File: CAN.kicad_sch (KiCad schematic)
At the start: 17 parts, among them J8 CAN_IN, J9 CAN_OUT, U6 ADM3055E, U7 CDSOT23-T24CAN

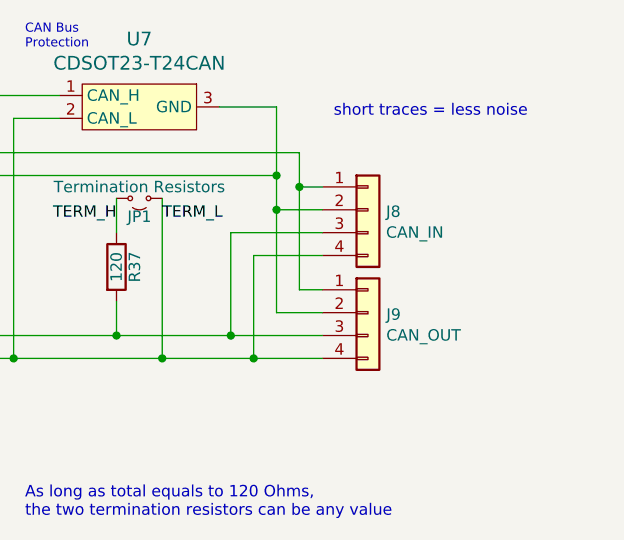
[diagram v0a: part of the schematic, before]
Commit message: parts sheet and cost estimate
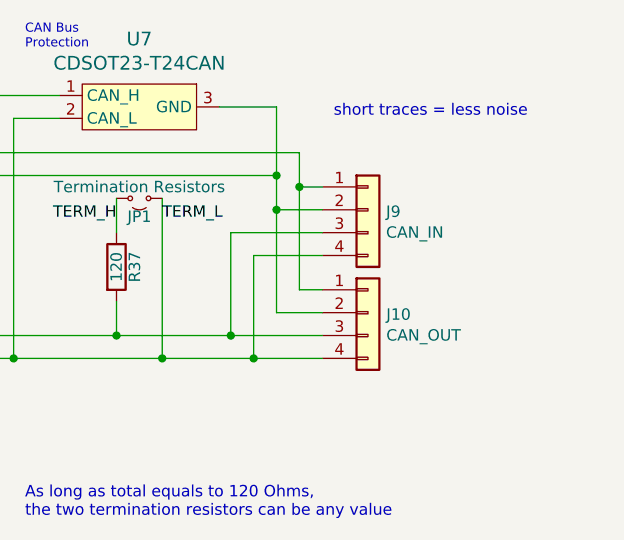
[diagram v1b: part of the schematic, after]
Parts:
- J10: renamed from J9; footprint UTSVT_Connectors:Molex_MicroFit3.0_1x4xP3.00mm_PolarizingPeg_Vertical -> utsvt-conn:Molex_MicroFit3.0_1x4xP3.00mm_PolarizingPeg_Vertical
- J9: renamed from J8; footprint UTSVT_Connectors:Molex_MicroFit3.0_1x4xP3.00mm_PolarizingPeg_Vertical -> utsvt-conn:Molex_MicroFit3.0_1x4xP3.00mm_PolarizingPeg_Vertical
- U6: footprint UTSVT_ICs:SOIC-20W_7.5x15.4mm_Pitch1.27mm -> utsvt-ics:SOIC-20W_7.5x15.4mm_Pitch1.27mm
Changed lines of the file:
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@@
 		(on_board yes)
 		(dnp no)
-		(property "Reference" "J9"
+		(property "Reference" "J10"
 			(at 221.742 92.9132 0)
 			(effects
@@
 			)
 		)
-		(property "Footprint" "UTSVT_Connectors:Molex_MicroFit3.0_1x4xP3.00mm_PolarizingPeg_Vertical"
+		(property "Footprint" "utsvt-conn:Molex_MicroFit3.0_1x4xP3.00mm_PolarizingPeg_Vertical"
 			(at 219.71 92.71 0)
 			(effects
@@
 			(project "ActivePrecharge"
 				(path "/b9847a31-2b3b-47ca-9561-fab506416f6d/a2982df7-4a65-4a2b-8298-6a7a639680dd"
-					(reference "J9")
+					(reference "J10")
 					(unit 1)
 				)
@@
 			)
 		)
-		(property "Footprint" "UTSVT_ICs:SOIC-20W_7.5x15.4mm_Pitch1.27mm"
+		(property "Footprint" "utsvt-ics:SOIC-20W_7.5x15.4mm_Pitch1.27mm"
 			(at 99.06 86.36 0)
 			(effects
@@
 		(on_board yes)
 		(dnp no)
-		(property "Reference" "J8"
+		(property "Reference" "J9"
 			(at 221.7166 81.4832 0)
 			(effects
@@
 			)
 		)
-		(property "Footprint" "UTSVT_Connectors:Molex_MicroFit3.0_1x4xP3.00mm_PolarizingPeg_Vertical"
+		(property "Footprint" "utsvt-conn:Molex_MicroFit3.0_1x4xP3.00mm_PolarizingPeg_Vertical"
 			(at 219.71 81.28 0)
 			(effects
@@
 			(project "ActivePrecharge"
 				(path "/b9847a31-2b3b-47ca-9561-fab506416f6d/a2982df7-4a65-4a2b-8298-6a7a639680dd"
-					(reference "J8")
+					(reference "J9")
 					(unit 1)
 				)

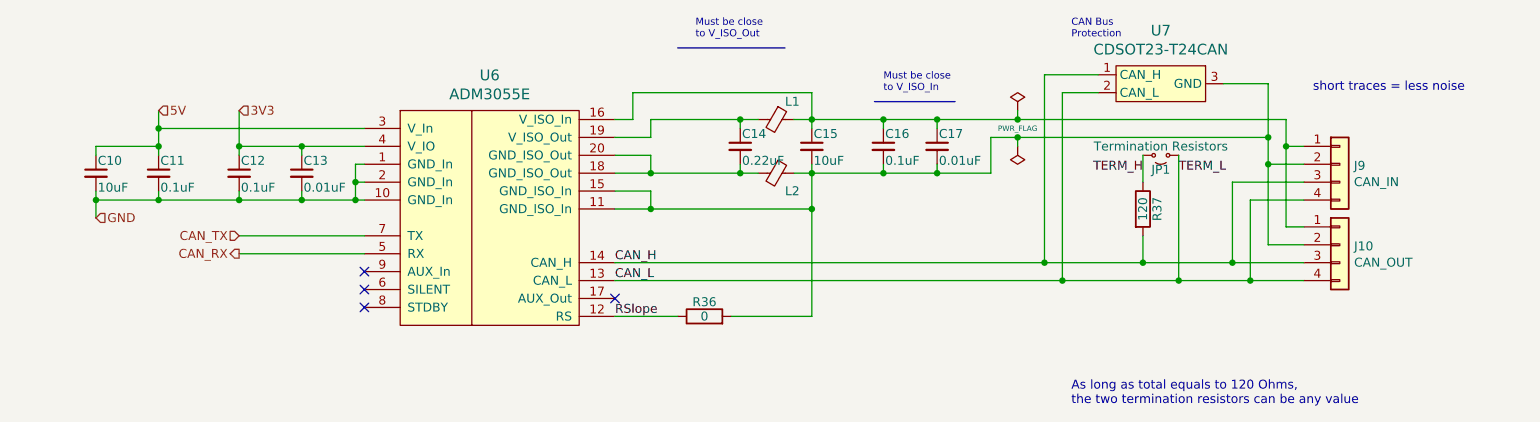
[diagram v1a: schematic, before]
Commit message: started on HV layout
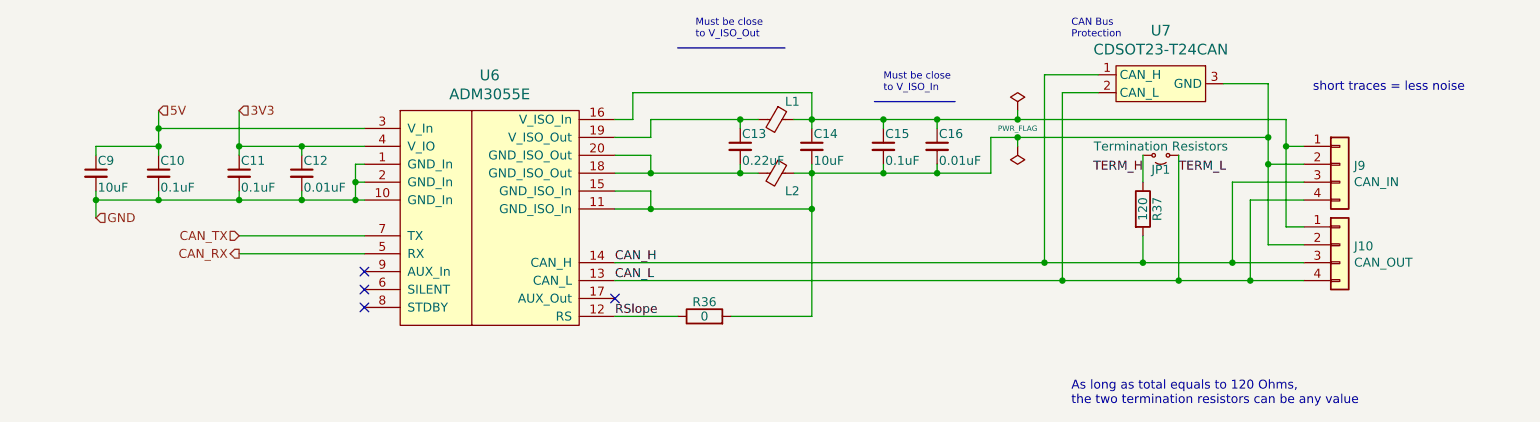
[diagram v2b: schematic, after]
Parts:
- renumbered C11 to C10, C12 to C11, C13 to C12, C14 to C13, C15 to C14, C16 to C15, C17 to C16, C10 to C9
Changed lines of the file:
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@@
 		(on_board yes)
 		(dnp no)
-		(property "Reference" "C13"
+		(property "Reference" "C12"
 			(at 72.644 80.772 0)
 			(effects
@@
 			(project "ActivePrecharge"
 				(path "/b9847a31-2b3b-47ca-9561-fab506416f6d/a2982df7-4a65-4a2b-8298-6a7a639680dd"
-					(reference "C13")
+					(reference "C12")
 					(unit 1)
 				)
@@
 		(on_board yes)
 		(dnp no)
-		(property "Reference" "C17"
+		(property "Reference" "C16"
 			(at 162.814 76.962 0)
 			(effects
@@
 			(project "ActivePrecharge"
 				(path "/b9847a31-2b3b-47ca-9561-fab506416f6d/a2982df7-4a65-4a2b-8298-6a7a639680dd"
-					(reference "C17")
+					(reference "C16")
 					(unit 1)
 				)
@@
 		(on_board yes)
 		(dnp no)
-		(property "Reference" "C10"
+		(property "Reference" "C9"
 			(at 43.434 80.772 0)
 			(effects
@@
 			(project "ActivePrecharge"
 				(path "/b9847a31-2b3b-47ca-9561-fab506416f6d/a2982df7-4a65-4a2b-8298-6a7a639680dd"
-					(reference "C10")
+					(reference "C9")
 					(unit 1)
 				)
@@
 		(on_board yes)
 		(dnp no)
-		(property "Reference" "C12"
+		(property "Reference" "C11"
 			(at 63.754 80.772 0)
 			(effects
@@
 			(project "ActivePrecharge"
 				(path "/b9847a31-2b3b-47ca-9561-fab506416f6d/a2982df7-4a65-4a2b-8298-6a7a639680dd"
-					(reference "C12")
+					(reference "C11")
 					(unit 1)
 				)
@@
 		(on_board yes)
 		(dnp no)
-		(property "Reference" "C11"
+		(property "Reference" "C10"
 			(at 52.324 80.772 0)
 			(effects
@@
 			(project "ActivePrecharge"
 				(path "/b9847a31-2b3b-47ca-9561-fab506416f6d/a2982df7-4a65-4a2b-8298-6a7a639680dd"
-					(reference "C11")
+					(reference "C10")
 					(unit 1)
 				)
@@
 		(on_board yes)
 		(dnp no)
-		(property "Reference" "C14"
+		(property "Reference" "C13"
 			(at 134.874 76.962 0)
 			(effects
@@
 			(project "ActivePrecharge"
 				(path "/b9847a31-2b3b-47ca-9561-fab506416f6d/a2982df7-4a65-4a2b-8298-6a7a639680dd"
-					(reference "C14")
+					(reference "C13")
 					(unit 1)
 				)
@@
 		(on_board yes)
 		(dnp no)
-		(property "Reference" "C16"
+		(property "Reference" "C15"
 			(at 155.194 76.962 0)
 			(effects
@@
 			(project "ActivePrecharge"
 				(path "/b9847a31-2b3b-47ca-9561-fab506416f6d/a2982df7-4a65-4a2b-8298-6a7a639680dd"
-					(reference "C16")
+					(reference "C15")
 					(unit 1)
 				)
@@
 		(on_board yes)
 		(dnp no)
-		(property "Reference" "C15"
+		(property "Reference" "C14"
 			(at 145.034 76.962 0)
 			(effects
@@
 			(project "ActivePrecharge"
 				(path "/b9847a31-2b3b-47ca-9561-fab506416f6d/a2982df7-4a65-4a2b-8298-6a7a639680dd"
-					(reference "C15")
+					(reference "C14")
 					(unit 1)
 				)

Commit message: fixed lakshay and ravi comments, renamed signals to be more readable, further worked on HV side layout
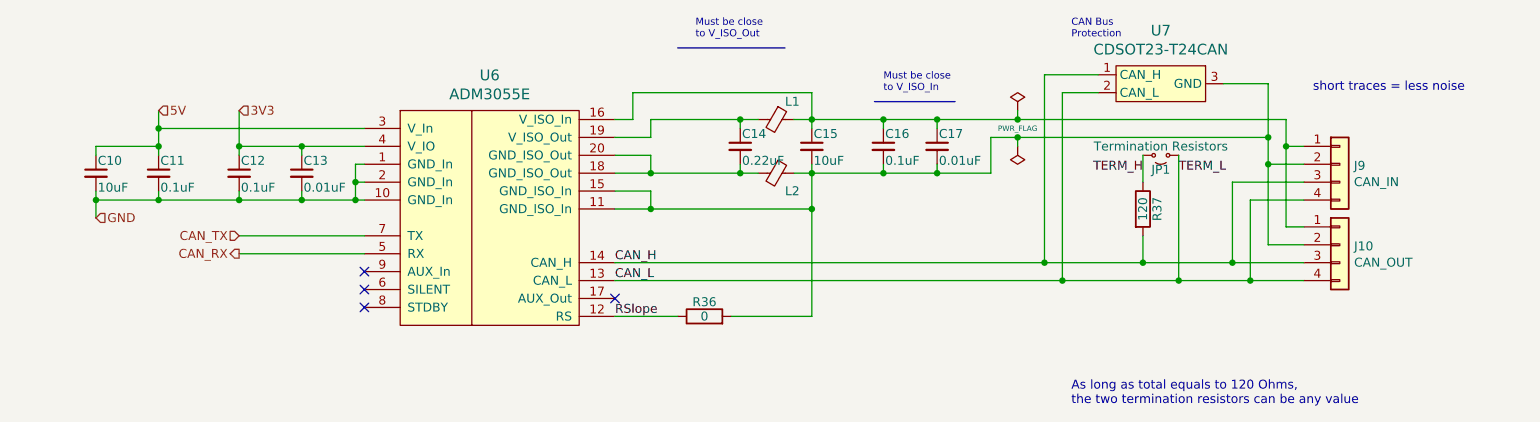
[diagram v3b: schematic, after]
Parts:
- renumbered C9 to C10, C10 to C11, C11 to C12, C12 to C13, C13 to C14, C14 to C15, C15 to C16, C16 to C17
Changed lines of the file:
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@@
 		(on_board yes)
 		(dnp no)
-		(property "Reference" "C12"
+		(property "Reference" "C13"
 			(at 72.644 80.772 0)
 			(effects
@@
 			(project "ActivePrecharge"
 				(path "/b9847a31-2b3b-47ca-9561-fab506416f6d/a2982df7-4a65-4a2b-8298-6a7a639680dd"
-					(reference "C12")
+					(reference "C13")
 					(unit 1)
 				)
@@
 		(on_board yes)
 		(dnp no)
-		(property "Reference" "C16"
+		(property "Reference" "C17"
 			(at 162.814 76.962 0)
 			(effects
@@
 			(project "ActivePrecharge"
 				(path "/b9847a31-2b3b-47ca-9561-fab506416f6d/a2982df7-4a65-4a2b-8298-6a7a639680dd"
-					(reference "C16")
+					(reference "C17")
 					(unit 1)
 				)
@@
 		(on_board yes)
 		(dnp no)
-		(property "Reference" "C9"
+		(property "Reference" "C10"
 			(at 43.434 80.772 0)
 			(effects
@@
 			(project "ActivePrecharge"
 				(path "/b9847a31-2b3b-47ca-9561-fab506416f6d/a2982df7-4a65-4a2b-8298-6a7a639680dd"
-					(reference "C9")
+					(reference "C10")
 					(unit 1)
 				)
@@
 		(on_board yes)
 		(dnp no)
-		(property "Reference" "C11"
+		(property "Reference" "C12"
 			(at 63.754 80.772 0)
 			(effects
@@
 			(project "ActivePrecharge"
 				(path "/b9847a31-2b3b-47ca-9561-fab506416f6d/a2982df7-4a65-4a2b-8298-6a7a639680dd"
-					(reference "C11")
+					(reference "C12")
 					(unit 1)
 				)
@@
 		(on_board yes)
 		(dnp no)
-		(property "Reference" "C10"
+		(property "Reference" "C11"
 			(at 52.324 80.772 0)
 			(effects
@@
 			(project "ActivePrecharge"
 				(path "/b9847a31-2b3b-47ca-9561-fab506416f6d/a2982df7-4a65-4a2b-8298-6a7a639680dd"
-					(reference "C10")
+					(reference "C11")
 					(unit 1)
 				)
@@
 		(on_board yes)
 		(dnp no)
-		(property "Reference" "C13"
+		(property "Reference" "C14"
 			(at 134.874 76.962 0)
 			(effects
@@
 			(project "ActivePrecharge"
 				(path "/b9847a31-2b3b-47ca-9561-fab506416f6d/a2982df7-4a65-4a2b-8298-6a7a639680dd"
-					(reference "C13")
+					(reference "C14")
 					(unit 1)
 				)
@@
 		(on_board yes)
 		(dnp no)
-		(property "Reference" "C15"
+		(property "Reference" "C16"
 			(at 155.194 76.962 0)
 			(effects
@@
 			(project "ActivePrecharge"
 				(path "/b9847a31-2b3b-47ca-9561-fab506416f6d/a2982df7-4a65-4a2b-8298-6a7a639680dd"
-					(reference "C15")
+					(reference "C16")
 					(unit 1)
 				)
@@
 		(on_board yes)
 		(dnp no)
-		(property "Reference" "C14"
+		(property "Reference" "C15"
 			(at 145.034 76.962 0)
 			(effects
@@
 			(project "ActivePrecharge"
 				(path "/b9847a31-2b3b-47ca-9561-fab506416f6d/a2982df7-4a65-4a2b-8298-6a7a639680dd"
-					(reference "C14")
+					(reference "C15")
 					(unit 1)
 				)

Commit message: end of workday, will work on more tonight
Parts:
- renumbered J9 to J8, J10 to J9
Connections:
- net CAN_H: now also J8.2 (Pin_2), J9.2 (Pin_2); no longer J8.3 (Pin_3), J9.3 (Pin_3)
- net CAN_L: now also J8.1 (Pin_1), J9.1 (Pin_1); no longer J8.4 (Pin_4), J9.4 (Pin_4)
- net at C15.1, C16.1, C17.1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: now also J8.4 (Pin_4), J9.4 (Pin_4); no longer J8.1 (Pin_1), J9.1 (Pin_1)
- net at C15.2, C16.2, C17.2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: now also J8.3 (Pin_3), J9.3 (Pin_3); no longer J8.2 (Pin_2), J9.2 (Pin_2)
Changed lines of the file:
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@@
 	(symbol
 		(lib_id "Connector_Generic:Conn_01x04")
-		(at 219.71 92.71 0)
+		(at 219.71 95.25 0)
+		(mirror x)
 		(unit 1)
 		(exclude_from_sim no)
@@
 		(on_board yes)
 		(dnp no)
-		(property "Reference" "J10"
-			(at 221.742 92.9132 0)
+		(property "Reference" "J9"
+			(at 221.742 95.0468 0)
 			(effects
 				(font
@@
 		)
 		(property "Value" "CAN_OUT"
-			(at 221.742 95.2246 0)
+			(at 221.742 92.7354 0)
 			(effects
 				(font
@@
 		)
 		(property "Footprint" "utsvt-conn:Molex_MicroFit3.0_1x4xP3.00mm_PolarizingPeg_Vertical"
-			(at 219.71 92.71 0)
+			(at 219.71 95.25 0)
 			(effects
 				(font
@@
 		)
 		(property "Datasheet" "~"
-			(at 219.71 92.71 0)
+			(at 219.71 95.25 0)
 			(effects
 				(font
@@
 		)
 		(property "Description" "Generic connector, single row, 01x04, script generated (kicad-library-utils/schlib/autogen/connector/)"
-			(at 219.71 92.71 0)
+			(at 219.71 95.25 0)
 			(effects
 				(font
@@
 		)
 		(property "Id" ""
-			(at 219.71 92.71 0)
+			(at 219.71 95.25 0)
 			(effects
 				(font
@@
 		)
 		(property "Vds" ""
-			(at 219.71 92.71 0)
+			(at 219.71 95.25 0)
 			(effects
 				(font
@@
 		)
 		(property "Digikey" ""
-			(at 219.71 92.71 0)
+			(at 219.71 95.25 0)
 			(effects
 				(font
@@
 		)
 		(property "P/N" "436500244"
-			(at 219.71 92.71 0)
+			(at 219.71 95.25 0)
 			(effects
 				(font
@@
 			(project "ActivePrecharge"
 				(path "/b9847a31-2b3b-47ca-9561-fab506416f6d/a2982df7-4a65-4a2b-8298-6a7a639680dd"
-					(reference "J10")
+					(reference "J9")
 					(unit 1)
 				)
@@
 	(symbol
 		(lib_id "Connector_Generic:Conn_01x04")
-		(at 219.71 81.28 0)
+		(at 219.71 83.82 0)
+		(mirror x)
 		(unit 1)
 		(exclude_from_sim no)
@@
 		(on_board yes)
 		(dnp no)
-		(property "Reference" "J9"
-			(at 221.7166 81.4832 0)
+		(property "Reference" "J8"
+			(at 221.7166 83.6168 0)
 			(effects
 				(font
@@
 		)
 		(property "Value" "CAN_IN"
-			(at 221.7166 83.7946 0)
+			(at 221.7166 81.3054 0)
 			(effects
 				(font
@@
 		)
 		(property "Footprint" "utsvt-conn:Molex_MicroFit3.0_1x4xP3.00mm_PolarizingPeg_Vertical"
-			(at 219.71 81.28 0)
+			(at 219.71 83.82 0)
 			(effects
 				(font
@@
 		)
 		(property "Datasheet" "~"
-			(at 219.71 81.28 0)
+			(at 219.71 83.82 0)
 			(effects
 				(font
@@
 		)
 		(property "Description" "Generic connector, single row, 01x04, script generated (kicad-library-utils/schlib/autogen/connector/)"
-			(at 219.71 81.28 0)
+			(at 219.71 83.82 0)
 			(effects
 				(font
@@
 		)
 		(property "Id" ""
-			(at 219.71 81.28 0)
+			(at 219.71 83.82 0)
 			(effects
 				(font
@@
 		)
 		(property "Vds" ""
-			(at 219.71 81.28 0)
+			(at 219.71 83.82 0)
 			(effects
 				(font
@@
 		)
 		(property "Digikey" ""
-			(at 219.71 81.28 0)
+			(at 219.71 83.82 0)
 			(effects
 				(font
@@
 		)
 		(property "P/N" "436500244"
-			(at 219.71 81.28 0)
+			(at 219.71 83.82 0)
 			(effects
 				(font
@@
 			(project "ActivePrecharge"
 				(path "/b9847a31-2b3b-47ca-9561-fab506416f6d/a2982df7-4a65-4a2b-8298-6a7a639680dd"
-					(reference "J9")
+					(reference "J8")
 					(unit 1)
 				)

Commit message: adjusted based off ravi and frank
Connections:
- net CAN_H: now also J8.3 (Pin_3), J9.3 (Pin_3); no longer J8.2 (Pin_2), J9.2 (Pin_2)
- net CAN_L: now also J8.4 (Pin_4), J9.4 (Pin_4); no longer J8.1 (Pin_1), J9.1 (Pin_1)
- net at C15.2, C16.2, C17.2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: now also J8.2 (Pin_2), J9.2 (Pin_2); no longer J8.3 (Pin_3), J9.3 (Pin_3)
- net at C15.1, C16.1, C17.1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: now also J8.1 (Pin_1), J9.1 (Pin_1); no longer J8.4 (Pin_4), J9.4 (Pin_4)
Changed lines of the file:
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@@
 	(symbol
 		(lib_id "Connector_Generic:Conn_01x04")
-		(at 219.71 95.25 0)
-		(mirror x)
+		(at 219.71 92.71 0)
 		(unit 1)
 		(exclude_from_sim no)
@@
 		(dnp no)
 		(property "Reference" "J9"
-			(at 221.742 95.0468 0)
+			(at 221.742 92.9132 0)
 			(effects
 				(font
@@
 		)
 		(property "Value" "CAN_OUT"
-			(at 221.742 92.7354 0)
+			(at 221.742 95.2246 0)
 			(effects
 				(font
@@
 		)
 		(property "Footprint" "utsvt-conn:Molex_MicroFit3.0_1x4xP3.00mm_PolarizingPeg_Vertical"
-			(at 219.71 95.25 0)
+			(at 219.71 92.71 0)
 			(effects
 				(font
@@
 		)
 		(property "Datasheet" "~"
-			(at 219.71 95.25 0)
+			(at 219.71 92.71 0)
 			(effects
 				(font
@@
 		)
 		(property "Description" "Generic connector, single row, 01x04, script generated (kicad-library-utils/schlib/autogen/connector/)"
-			(at 219.71 95.25 0)
+			(at 219.71 92.71 0)
 			(effects
 				(font
@@
 		)
 		(property "Id" ""
-			(at 219.71 95.25 0)
+			(at 219.71 92.71 0)
 			(effects
 				(font
@@
 		)
 		(property "Vds" ""
-			(at 219.71 95.25 0)
+			(at 219.71 92.71 0)
 			(effects
 				(font
@@
 		)
 		(property "Digikey" ""
-			(at 219.71 95.25 0)
+			(at 219.71 92.71 0)
 			(effects
 				(font
@@
 		)
 		(property "P/N" "436500244"
-			(at 219.71 95.25 0)
+			(at 219.71 92.71 0)
 			(effects
 				(font
@@
 	(symbol
 		(lib_id "Connector_Generic:Conn_01x04")
-		(at 219.71 83.82 0)
-		(mirror x)
+		(at 219.71 81.28 0)
 		(unit 1)
 		(exclude_from_sim no)
@@
 		(dnp no)
 		(property "Reference" "J8"
-			(at 221.7166 83.6168 0)
+			(at 221.7166 81.4832 0)
 			(effects
 				(font
@@
 		)
 		(property "Value" "CAN_IN"
-			(at 221.7166 81.3054 0)
+			(at 221.7166 83.7946 0)
 			(effects
 				(font
@@
 		)
 		(property "Footprint" "utsvt-conn:Molex_MicroFit3.0_1x4xP3.00mm_PolarizingPeg_Vertical"
-			(at 219.71 83.82 0)
+			(at 219.71 81.28 0)
 			(effects
 				(font
@@
 		)
 		(property "Datasheet" "~"
-			(at 219.71 83.82 0)
+			(at 219.71 81.28 0)
 			(effects
 				(font
@@
 		)
 		(property "Description" "Generic connector, single row, 01x04, script generated (kicad-library-utils/schlib/autogen/connector/)"
-			(at 219.71 83.82 0)
+			(at 219.71 81.28 0)
 			(effects
 				(font
@@
 		)
 		(property "Id" ""
-			(at 219.71 83.82 0)
+			(at 219.71 81.28 0)
 			(effects
 				(font
@@
 		)
 		(property "Vds" ""
-			(at 219.71 83.82 0)
+			(at 219.71 81.28 0)
 			(effects
 				(font
@@
 		)
 		(property "Digikey" ""
-			(at 219.71 83.82 0)
+			(at 219.71 81.28 0)
 			(effects
 				(font
@@
 		)
 		(property "P/N" "436500244"
-			(at 219.71 83.82 0)
-			(effects
-				(font
+			(at 219.71 81.28 0)
+			(effects
+				(font

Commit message: layout finalized just need to make labels prettier
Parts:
- added J10: Conn_01x02, Connector_PinHeader_2.54mm:PinHeader_1x02_P2.54mm_Vertical, symbol Connector_Generic:Conn_01x02
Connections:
- net CAN_RX: now also J10.2 (Pin_2)
- net CAN_TX: now also J10.1 (Pin_1)
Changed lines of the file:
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@@
+	(wire
+		(pts
+			(xy 46.99 100.33) (xy 43.18 100.33)
+		)
+		(stroke
+			(width 0)
+			(type default)
+		)
+	)
 	(wire
 		(pts
@@
 		(pts
 			(xy 119.38 74.93) (xy 116.84 74.93)
+		)
+		(stroke
+			(width 0)
+			(type default)
+		)
+	)
+	(wire
+		(pts
+			(xy 46.99 102.87) (xy 43.18 102.87)
 		)
 		(stroke
@@
 		(shape input)
 		(at 52.07 73.66 0)
+		(fields_autoplaced yes)
+		(effects
+			(font
+				(size 1.27 1.27)
+			)
+			(justify left)
+		)
+	)
+	(hierarchical_label "CAN_RX"
+		(shape output)
+		(at 46.99 102.87 0)
+		(fields_autoplaced yes)
+		(effects
+			(font
+				(size 1.27 1.27)
+			)
+			(justify left)
+		)
+	)
+	(hierarchical_label "CAN_TX"
+		(shape input)
+		(at 46.99 100.33 0)
 		(fields_autoplaced yes)
 		(effects
@@
 					(unit 1)
 				)
+			)
+		)
+	)
+	(symbol
+		(lib_id "Connector_Generic:Conn_01x02")
+		(at 38.1 100.33 0)
+		(mirror y)
+		(unit 1)
+		(exclude_from_sim no)
+		(in_bom yes)
+		(on_board yes)
+		(dnp no)
+		(fields_autoplaced yes)
+		(property "Reference" "J10"
+			(at 38.1 93.98 0)
+			(effects
+				(font
+					(size 1.27 1.27)
+				)
+			)
+		)
+		(property "Value" "Conn_01x02"
+			(at 38.1 96.52 0)
+			(effects
+				(font
+					(size 1.27 1.27)
+				)
+			)
+		)
+		(property "Footprint" "Connector_PinHeader_2.54mm:PinHeader_1x02_P2.54mm_Vertical"
+			(at 38.1 100.33 0)
+			(effects
+				(font
+					(size 1.27 1.27)
+				)
+				(hide yes)
+			)
+		)
+		(property "Datasheet" "~"
+			(at 38.1 100.33 0)
+			(effects
+				(font
+					(size 1.27 1.27)
+				)
+				(hide yes)
+			)
+		)
+		(property "Description" "Generic connector, single row, 01x02, script generated (kicad-library-utils/schlib/autogen/connector/)"
+			(at 38.1 100.33 0)
+			(effects
+				(font
+					(size 1.27 1.27)
+				)
+				(hide yes)
+			)
+		)
+		(pin "2"
+		)
+		(pin "1"
+		)
+		(instances
+			(project ""
+				(path "/b9847a31-2b3b-47ca-9561-fab506416f6d/a2982df7-4a65-4a2b-8298-6a7a639680dd"
+					(reference "J10")
+					(unit 1)
+				)
